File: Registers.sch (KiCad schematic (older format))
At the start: 28 parts, among them U20 74HC574, U21 74HC574, U22 74HC574, U23 74HC574, U24 74HC574, U25 74HC574, U26 74HC574, U27 74HC574, U29 74HC27, U30 74HC27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

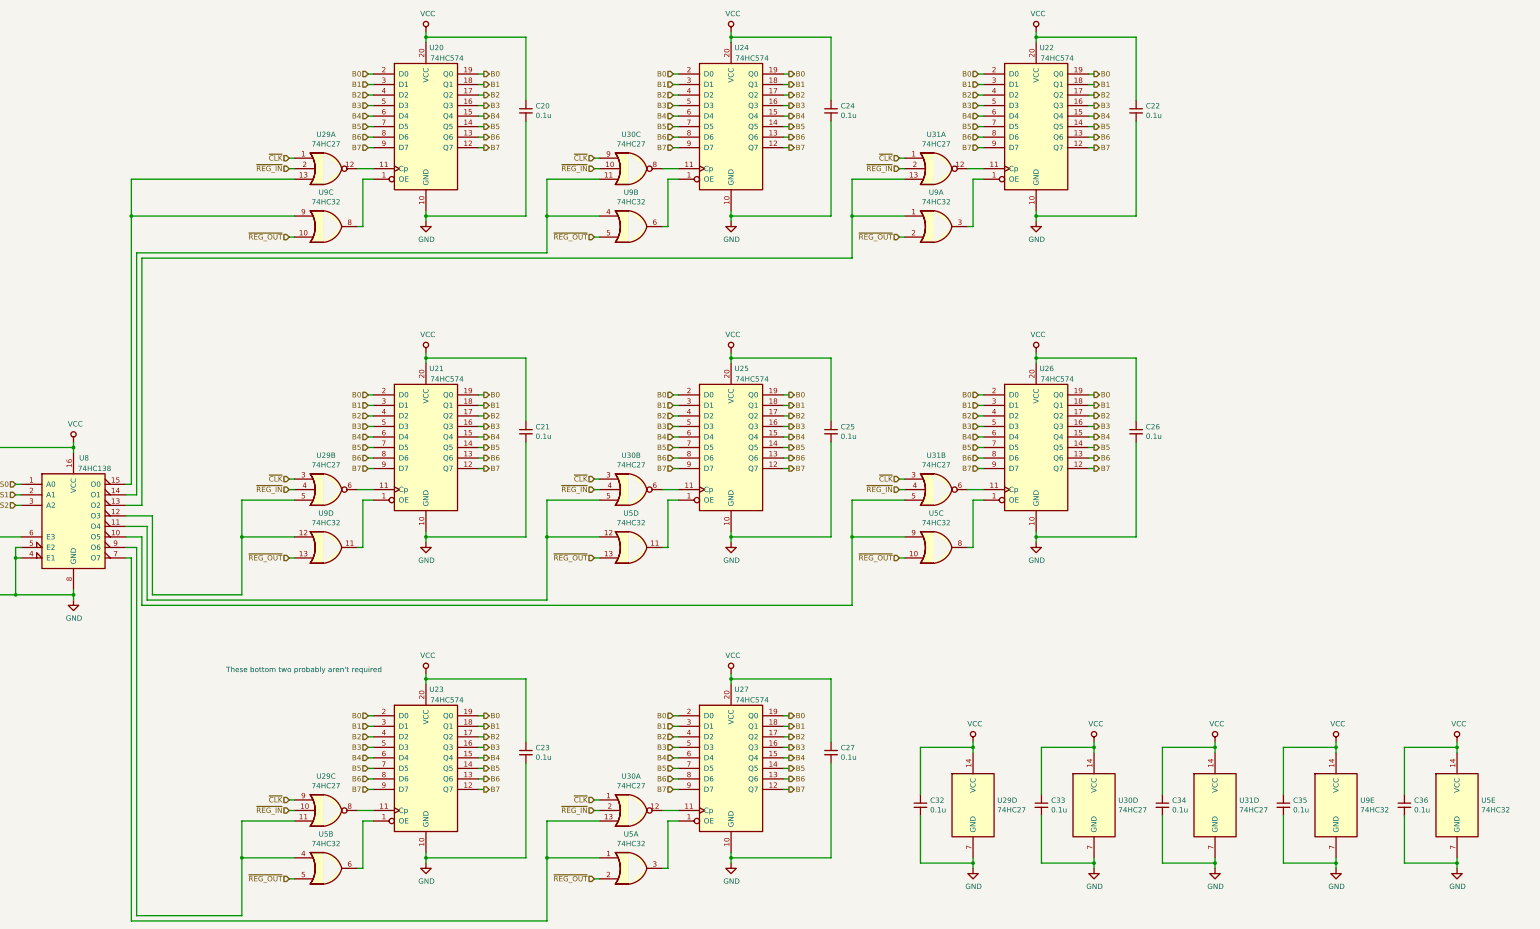
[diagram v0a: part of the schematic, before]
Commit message: Migrated old device part numbers to SN74 LS or HCT series
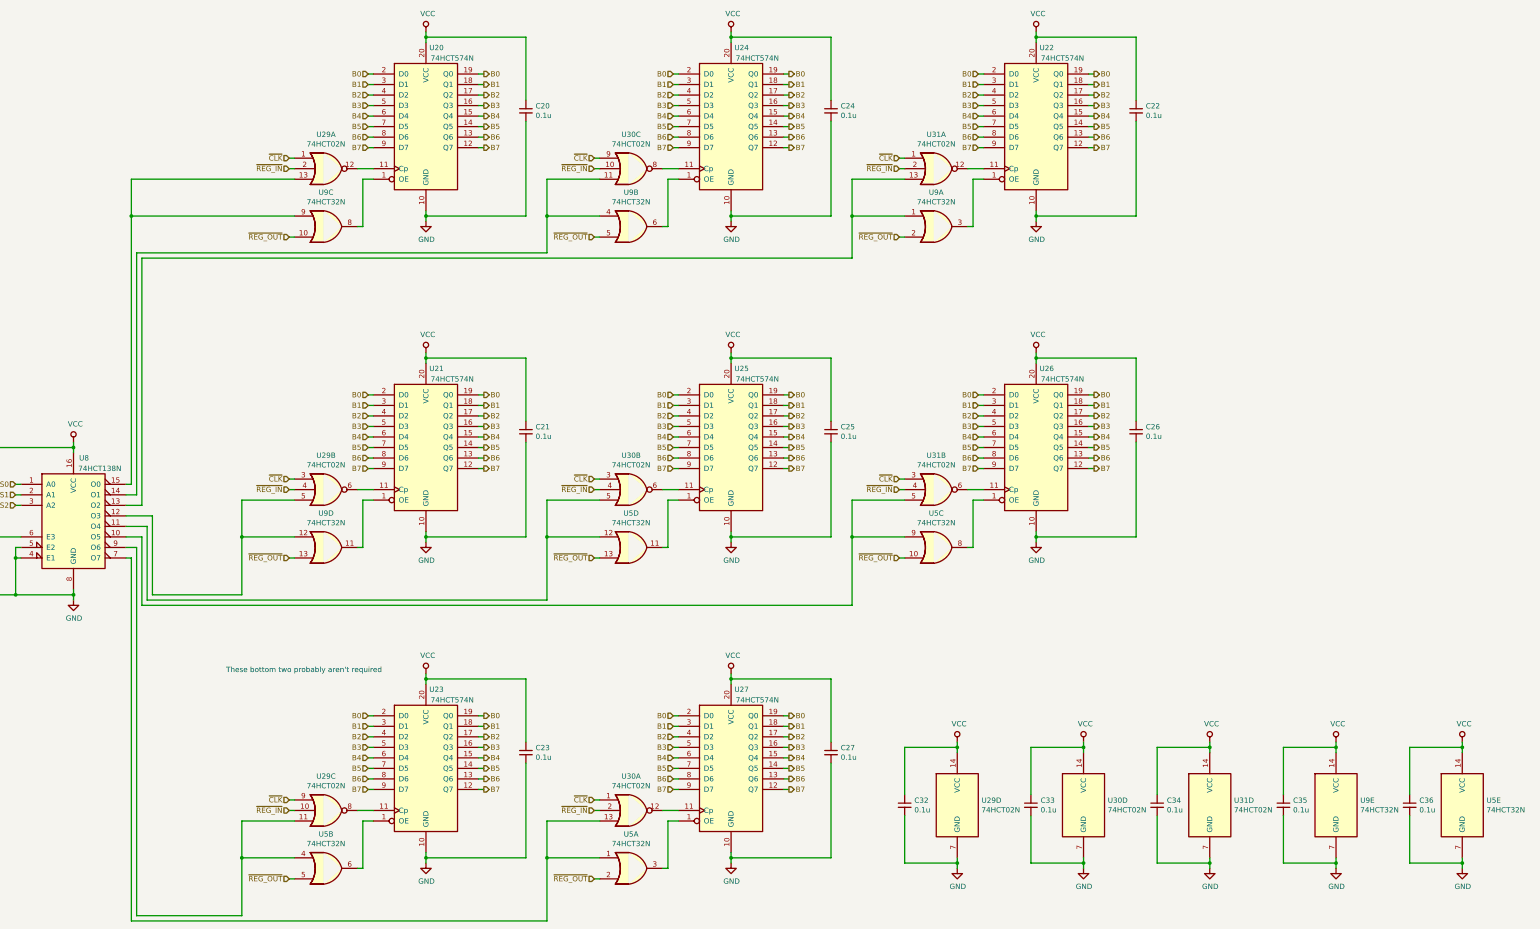
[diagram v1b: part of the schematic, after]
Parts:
- U20, U21, U22, U23, U24, U25, U26, U27: value 74HC574 -> 74HCT574N
- U29, U30, U31: value 74HC27 -> 74HCT02N
- U5, U9: value 74HC32 -> 74HCT32N
- U8: value 74HC138 -> 74HCT138N
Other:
- moved on the sheet: C32, C33, C34, C36, U29D, U30D, U31D, U5E

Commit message: Remote work
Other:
- note added: "Register Arrays"
- note added: "Register Selector"
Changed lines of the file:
@@
 	1    0    0    -1
 $EndComp
+Text Notes 975  6725 0    118  ~ 0
+Register Selector
+Text Notes 13550 4850 0    118  ~ 0
+Register Arrays
 $EndSCHEMATC

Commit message: Replaced all broken schematics with the up-to-date versions.  Some symbols missing.  This version will be the one created IRL except for the carry flag.
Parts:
- added U702: 74HCT08N, symbol Breadboard_CPU-rescue:74LS08-74xx
- added U703: 74HCT74N, symbol Breadboard_CPU-rescue:74LS74-74xx
- added U709: 74LS32, symbol Breadboard_CPU-rescue:74LS32-74xx
- added U710, U711, U721, U722: 74LS193, symbol Breadboard_CPU-rescue:74LS193-74xx
- added U717, U723: 74HCT541N, symbol Breadboard_CPU-rescue:74LS541-74xx
- C701: renamed from C31; symbol Device:C_Small -> Breadboard_CPU-rescue:C_Small-Device
- C702: renamed from C20; symbol Device:C_Small -> Breadboard_CPU-rescue:C_Small-Device
- C703: renamed from C21; symbol Device:C_Small -> Breadboard_CPU-rescue:C_Small-Device
- C704: renamed from C23; symbol Device:C_Small -> Breadboard_CPU-rescue:C_Small-Device
- C705: renamed from C24; symbol Device:C_Small -> Breadboard_CPU-rescue:C_Small-Device
- C706: renamed from C25; symbol Device:C_Small -> Breadboard_CPU-rescue:C_Small-Device
- C707: renamed from C27; symbol Device:C_Small -> Breadboard_CPU-rescue:C_Small-Device
- C708: renamed from C22; symbol Device:C_Small -> Breadboard_CPU-rescue:C_Small-Device
- C709: renamed from C26; symbol Device:C_Small -> Breadboard_CPU-rescue:C_Small-Device
- C710: renamed from C32; symbol Device:C_Small -> Breadboard_CPU-rescue:C_Small-Device
- C711: renamed from C33; symbol Device:C_Small -> Breadboard_CPU-rescue:C_Small-Device
- C712: renamed from C34; symbol Device:C_Small -> Breadboard_CPU-rescue:C_Small-Device
- C713: renamed from C35; symbol Device:C_Small -> Breadboard_CPU-rescue:C_Small-Device
- C714: renamed from C36; symbol Device:C_Small -> Breadboard_CPU-rescue:C_Small-Device
- U701: renamed from U8; symbol 74xx:74LS138 -> Breadboard_CPU-rescue:74LS138-74xx
- U704: renamed from U29; value 74HCT02N -> 74LS27; symbol 74xx:74LS27 -> Breadboard_CPU-rescue:74LS27-74xx
- U705, U713: renamed from U9; symbol 74xx:74LS32 -> Breadboard_CPU-rescue:74LS32-74xx
- U705, U713: renamed from U5; symbol 74xx:74LS32 -> Breadboard_CPU-rescue:74LS32-74xx
- U706: renamed from U20; symbol 74xx:74HCT574 -> Breadboard_CPU-rescue:74HCT574-74xx
- U707: renamed from U21; symbol 74xx:74HCT574 -> Breadboard_CPU-rescue:74HCT574-74xx
- U708: renamed from U23; symbol 74xx:74HCT574 -> Breadboard_CPU-rescue:74HCT574-74xx
- U712: renamed from U30; value 74HCT02N -> 74LS27; symbol 74xx:74LS27 -> Breadboard_CPU-rescue:74LS27-74xx
- U714: renamed from U24; symbol 74xx:74HCT574 -> Breadboard_CPU-rescue:74HCT574-74xx
- U715: renamed from U25; symbol 74xx:74HCT574 -> Breadboard_CPU-rescue:74HCT574-74xx
- U716: renamed from U27; symbol 74xx:74HCT574 -> Breadboard_CPU-rescue:74HCT574-74xx
- U718: renamed from U31; value 74HCT02N -> 74LS27; symbol 74xx:74LS27 -> Breadboard_CPU-rescue:74LS27-74xx
- U719: renamed from U22; symbol 74xx:74HCT574 -> Breadboard_CPU-rescue:74HCT574-74xx
- U720: renamed from U26; symbol 74xx:74HCT574 -> Breadboard_CPU-rescue:74HCT574-74xx
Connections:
- net B0: now also U710.15 (A), U717.18 (Y0), U721.15 (A), U723.18 (Y0)
- net B1: now also U710.1 (B), U717.17 (Y1), U721.1 (B), U723.17 (Y1)
- net B2: now also U710.10 (C), U717.16 (Y2), U721.10 (C), U723.16 (Y2)
- net B3: now also U710.9 (D), U717.15 (Y3), U721.9 (D), U723.15 (Y3)
- net B4: now also U711.15 (A), U717.14 (Y4), U722.15 (A), U723.14 (Y4)
- net B5: now also U711.1 (B), U717.13 (Y5), U722.1 (B), U723.13 (Y5)
- net B6: now also U711.10 (C), U717.12 (Y6), U722.10 (C), U723.12 (Y6)
- net B7: now also U711.9 (D), U717.11 (Y7), U722.9 (D), U723.11 (Y7)
- net GND: now also U702.7 (GND), U703.7 (GND), U709.7 (GND), U710.8 (GND), U711.8 (GND), U717.10 (GND), U721.8 (GND), U722.8 (GND), U723.10 (GND)
- net VCC: now also U702.14 (VCC), U703.10 (~S), U703.14 (VCC), U703.4 (~S), U709.14 (VCC), U710.16 (VCC), U711.16 (VCC), U717.20 (VCC), U721.16 (VCC), U722.16 (VCC), U723.20 (VCC)
- net ~CLK: now also U702.10, U702.13
- new net: U709.3, U710.11 (~LOAD), U711.11 (~LOAD)
- new net: U710.12 (~CO), U711.5 (UP)
- new net: U710.13 (~BO), U711.4 (DOWN)
- new net: U710.2 (QB), U717.3 (A1)
- new net: U710.3 (QA), U717.2 (A0)
- new net: U710.6 (QC), U717.4 (A2)
- new net: U710.7 (QD), U717.5 (A3)
- new net: U711.12 (~CO), U721.5 (UP)
- new net: U711.13 (~BO), U721.4 (DOWN)
- new net: U711.2 (QB), U717.7 (A5)
- new net: U711.3 (QA), U717.6 (A4)
- new net: U711.6 (QC), U717.8 (A6)
- new net: U711.7 (QD), U717.9 (A7)
- new net: U709.6, U721.11 (~LOAD), U722.11 (~LOAD)
- new net: U721.12 (~CO), U722.5 (UP)
- new net: U721.13 (~BO), U722.4 (DOWN)
- new net: U721.2 (QB), U723.3 (A1)
- new net: U721.3 (QA), U723.2 (A0)
- new net: U721.6 (QC), U723.4 (A2)
- new net: U721.7 (QD), U723.5 (A3)
- new net: U722.2 (QB), U723.7 (A5)
- new net: U722.3 (QA), U723.6 (A4)
- new net: U722.6 (QC), U723.8 (A6)
- new net: U722.7 (QD), U723.9 (A7)
- new net: U709.11, U717.1 (G1), U717.19 (G2)
- new net: U702.11, U703.3 (C)
- new net: U702.8, U703.11 (C)
- new net: U709.8, U723.1 (G1), U723.19 (G2)
- new net RST: U710.14 (CLR), U711.14 (CLR), U721.14 (CLR), U722.14 (CLR)
- new net SP_DEC: U710.4 (DOWN)
- new net SP_IN: U702.12
- new net SP_INC: U710.5 (UP)
- new net SP_OUT: U702.9
- new net ~RST: U703.1 (~R), U703.13 (~R)
- new net ~SP_EN_LD_HIGH: U703.5 (Q), U709.4
- new net ~SP_EN_LD_LOW: U703.2 (D), U703.6 (~Q), U709.1
- new net ~SP_EN_OUT_HIGH: U703.9 (Q), U709.10
- new net ~SP_EN_OUT_LOW: U703.12 (D), U703.8 (~Q), U709.13
- new net ~SP_IN: U709.2, U709.5
- new net ~SP_OUT: U709.12, U709.9
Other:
- note added: "Register file"
- note removed: "Register Arrays"
- moved on the sheet: C710, C711, C712, C713, C714, U704D, U705E, U712D, U713E, U718D

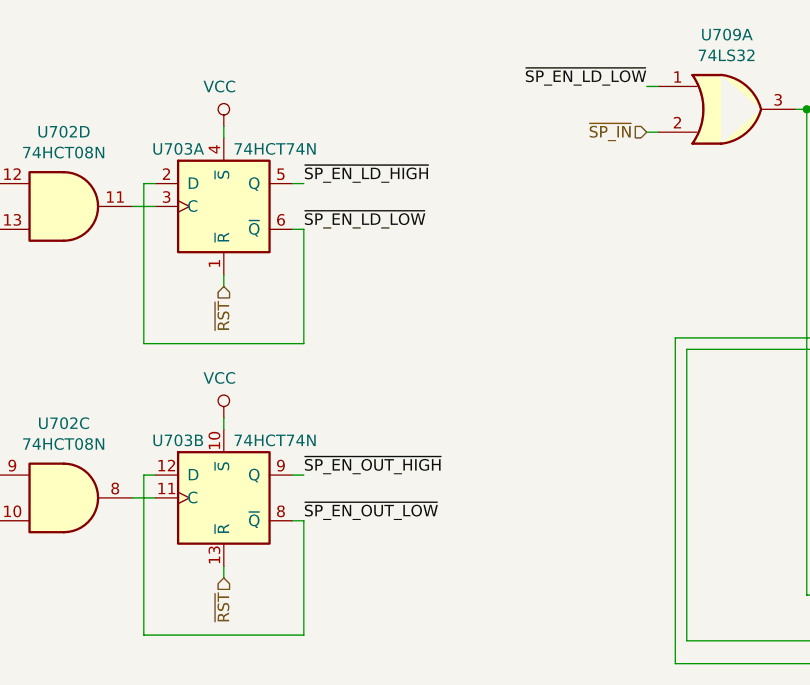
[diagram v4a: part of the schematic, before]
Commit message: Libraries re-imported.  Using rescue symbols still.  Adjusted multi-byte registers to use low-byte first.. applied this convention to all multi-byte registers for consistency.
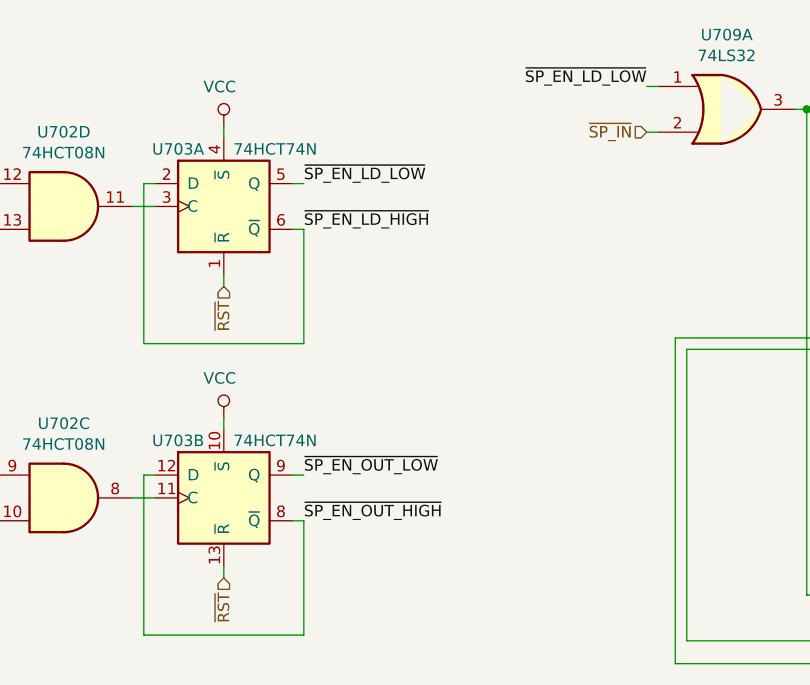
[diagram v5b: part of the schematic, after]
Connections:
- net ~SP_EN_LD_HIGH: now also U703.2 (D), U703.6 (~Q); no longer U703.5 (Q)
- net ~SP_EN_LD_LOW: now also U703.5 (Q); no longer U703.2 (D), U703.6 (~Q)
- net ~SP_EN_OUT_HIGH: now also U703.12 (D), U703.8 (~Q); no longer U703.9 (Q)
- net ~SP_EN_OUT_LOW: now also U703.9 (Q); no longer U703.12 (D), U703.8 (~Q)
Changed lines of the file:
@@
 Wire Wire Line
 	3650 12750 3700 12750
+Text Label 3700 12950 0    50   ~ 0
+~SP_EN_LD_HIGH
 Text Label 3700 12750 0    50   ~ 0
-~SP_EN_LD_HIGH
-Text Label 3700 12950 0    50   ~ 0
 ~SP_EN_LD_LOW
 Wire Wire Line
@@
 Wire Wire Line
 	3650 14025 3700 14025
+Text Label 3700 14225 0    50   ~ 0
+~SP_EN_OUT_HIGH
 Text Label 3700 14025 0    50   ~ 0
-~SP_EN_OUT_HIGH
-Text Label 3700 14225 0    50   ~ 0
 ~SP_EN_OUT_LOW
 Text HLabel 2300 12950 0    50   Input ~ 0

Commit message: Added REGS_ASSERT_RS0.  Added user referenceable CFL to solve issue of performing arithmetic on stack frame and global pointers.  TRAP routines will be created to perform ADD operations (leveraging JC/JNC) on SFP and GP.  uCode rev. 1 created in GDrive.
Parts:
- added Q? (x2): Q_NPN_CBE, symbol Breadboard_CPU-rescue:Q_NPN_CBE-Device
- added R? (x3): 10k, symbol Breadboard_CPU-rescue:R-Device
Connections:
- net GND: now also R?.2
- net RS0: now also R?.2; no longer U701.1 (A0)
- net VCC: now also Q?.1 (C), Q?.1 (C)
- new net: Q?.3 (E), Q?.3 (E), R?.1, U701.1 (A0)
- new net: Q?.2 (B), R?.1 (x2)
- new net REG_ASSERT_RS0: R?.2
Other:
- note removed: "These bottom two probably aren't required"
- moved on the sheet: C701, C702, C703, C704, C705, C706, C707, C708, C709, C710, C711, C712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

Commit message: Pre-removal of H/L byte deciding hardware
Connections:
- net SP_IN: no longer U702.12
- net SP_OUT: no longer U702.9
- net ~CLK: no longer U702.10, U702.13
- net ~SP_EN_LD_LOW: no longer U709.1
- net ~SPL_IN: now reaches U710.11 (~LOAD), U711.11 (~LOAD)
- net ~SPL_IN: no longer U709.3
- net ~SPH_IN: now reaches U721.11 (~LOAD), U722.11 (~LOAD)
- net ~SPH_IN: no longer U709.6
- net ~SPL_OUT: now reaches U717.1 (G1), U717.19 (G2)
- net ~SPL_OUT: no longer U709.11
- net ~SPH_OUT: now reaches U723.1 (G1), U723.19 (G2)
- net ~SPH_OUT: no longer U709.8
- net ~SP_IN: no longer names the net of U709.5
- net ~SP_IN: no longer U709.2
- net ~SP_OUT: no longer names the net of U709.9
- net ~SP_OUT: no longer U709.12
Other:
- note added: "If LOAD only happens on falling edge, create logic to pull LOAD low on CLK rise\n\nIf LOAD happens throughout, may need to make it synchronous with logic"
- moved on the sheet: U702C, U702D, U703A, U703B, U709A, U709B, U709C, U709D, U710, U711, U717, U721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

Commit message: Testing memory module
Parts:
- removed U703: 74HCT74N, symbol Breadboard_CPU-rescue:74LS74-74xx
- removed U709: 74LS32, symbol Breadboard_CPU-rescue:74LS32-74xx
- added C? (x4): 0.1u, symbol Device:C_Small
- added Q? (x4): Q_NPN_CBE, symbol Device:Q_NPN_CBE
- added R? (x4): 1, symbol Device:R
- added R? (x8): 1k, symbol Device:R
- added U? (x5): 74HCT08N, symbol Breadboard_CPU-rescue:74LS08-74xx
- added U? (x7): 74LS04, symbol Breadboard_CPU-rescue:74LS04-74xx
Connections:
- net ~SPL_IN is gone; now on an unnamed net: U710.11 (~LOAD), U711.11 (~LOAD)
- net GND: now also C?.2, C?.2, C?.2, C?.2, Q?.3 (E), Q?.3 (E), Q?.3 (E), Q?.3 (E), U?.7 (GND), U?.7 (GND)
- net SP_DEC: now also U702.9; no longer U710.4 (DOWN)
- net SP_INC: now also U702.1; no longer U710.5 (UP)
- net VCC: now also R?.1, R?.1, R?.1, R?.1, U?.14 (VCC), U?.14 (VCC)
- net ~SPH_OUT: now also U?.10
- net ~SPL_OUT: now also U?.12
- net at U710.12 (~CO), U711.5 (UP): now also U711.13 (~BO), U721.4 (DOWN)
- net at U711.12 (~CO), U721.5 (UP): now also Q?.1 (C), R?.2
- net at U702.11: now also R?.2
- net at U702.8: now also U702.12, U?.3
- net at U702.13: now also C?.1, R?.1
- net CLK: now reaches U702.10
- net CLK: now also U702.2, U?.2, U?.2
- net at U702.4: now also U702.3, U?.1
- net at U702.5: now also C?.1, R?.1
- net at U702.6: now also R?.2
- net ~SPH_IN: no longer names the net of U721.11 (~LOAD), U722.11 (~LOAD)
- net ~SPH_IN: now also Q?.1 (C), R?.2
- new net: C?.1, R?.1, U?.5 (x2)
- new net: R?.2, U?.6 (x3)
- new net: Q?.2 (B), R?.1 (x4)
- new net: U?.3, U?.4, U?.5
- new net: R?.2, U?.8
- new net: U?.3, U?.4, U?.9
- new net: R?.2, U?.2
- new net: R?.2, U?.4
- new net SPH_IN: U?.1
- new net SPH_OUT: U?.11
- new net SPL_IN: U?.1
- new net SPL_OUT: U?.13
- new net ~DOWN: Q?.1 (C), R?.2, U710.4 (DOWN)
- new net ~UP: Q?.1 (C), R?.2, U710.5 (UP)
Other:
- note removed: "If LOAD only happens on falling edge, create logic to pull LOAD low on CLK rise\n\nIf LOAD happens throughout, may need to make it synchronous with logic"
- moved on the sheet: C701, C702, C703, C704, C705, C706, C707, C708, C709, C710, C711, C712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
